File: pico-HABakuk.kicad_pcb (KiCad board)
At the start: 2 copper layers, 52 x 51.2 mm, 90 parts, among them J1 USB_B_Micro, J2 Ant+, J3 GPS Ant, J4 Ant-, J5 Solar, J6 Debug, J7 Super_Cap, Q1 BSS84, SW1 USB BOOT, SW2 RESET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

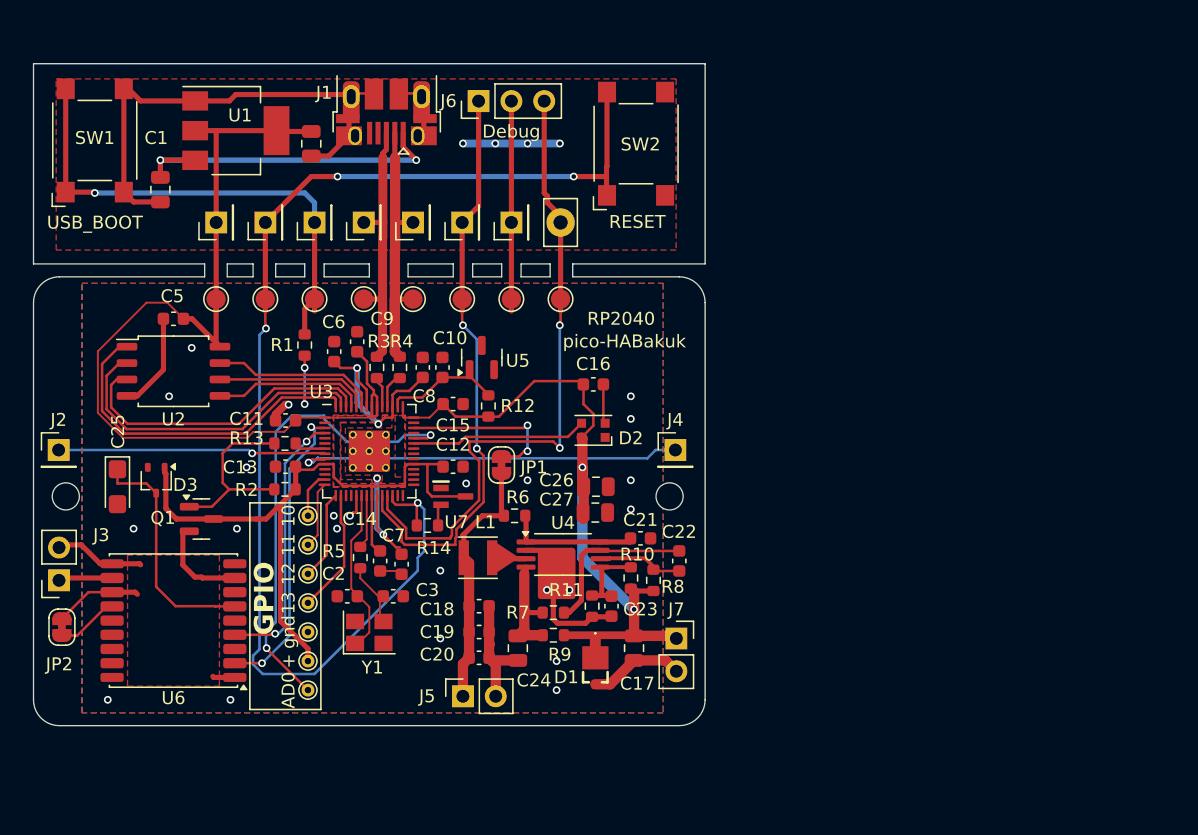
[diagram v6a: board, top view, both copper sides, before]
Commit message: Minor silkscreen edits
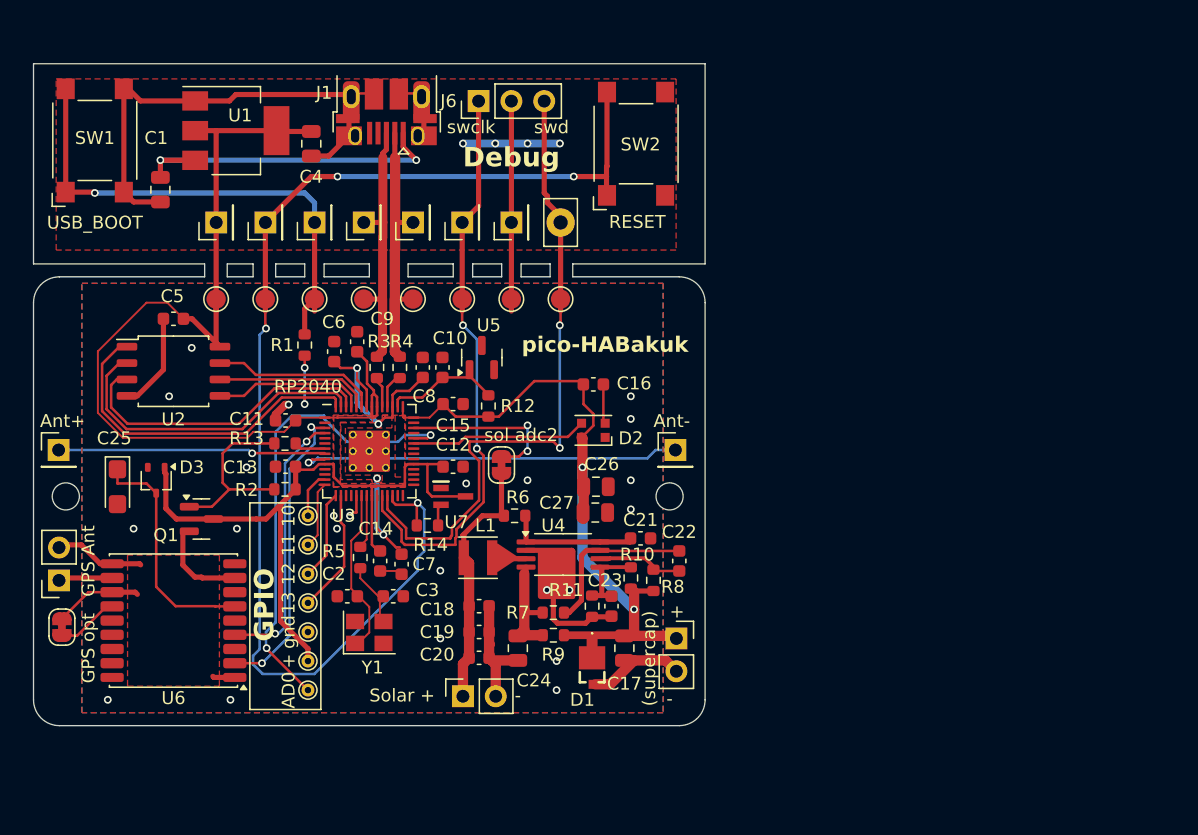
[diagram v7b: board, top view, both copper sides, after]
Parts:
- JP1: value Solar_voltage -> sol adc2
- JP2: value GPS+Glonass -> GPS opt
- moved C17 0.75 mm to (119.8, 115.2)
- moved D1 0.25 mm to (117.2, 116.0)
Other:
- rule pad_to_mask_clearance: 0.051 -> 0
- board text added: "(supercap)"
- board text added: "Solar +"
- board text added: "swclk"
- board text added: "swd"
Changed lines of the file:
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@@
 	)
 	(setup
-		(pad_to_mask_clearance 0.051)
-		(solder_mask_min_width 0.09)
+		(pad_to_mask_clearance 0)
 		(allow_soldermask_bridges_in_footprints no)
 		(aux_axis_origin 100 100)
@@
 			(disableapertmacros no)
 			(usegerberextensions no)
-			(usegerberattributes no)
+			(usegerberattributes yes)
 			(usegerberadvancedattributes no)
 			(creategerberjobfile no)
@@
 		(tags "capacitor")
 		(property "Reference" "C4"
-			(at 0 1.7 90)
+			(at 2.555 0.008 180)
 			(layer "F.SilkS")
-			(hide yes)
 			(effects
 				(font
@@
 		(tags "capacitor")
 		(property "Reference" "C14"
-			(at -3.25 1.588 0)
+			(at -2.5 0.338 0)
 			(layer "F.SilkS")
 			(effects
@@
 		(tags "capacitor")
 		(property "Reference" "C7"
-			(at -2.219 0.62 0)
+			(at 0 -1.75 0)
 			(layer "F.SilkS")
 			(effects
@@
 		(tags "capacitor")
 		(property "Reference" "C16"
-			(at 0 -1.578 0)
+			(at 3.152 -0.078 0)
 			(layer "F.SilkS")
 			(effects
@@
 		(tags "QFN DFN_QFN")
 		(property "Reference" "U3"
-			(at -3.71 -4.6 0)
+			(at -2 5 0)
 			(layer "F.SilkS")
 			(effects
@@
 	(footprint "Capacitor_SMD:C_0805_2012Metric"
 		(layer "F.Cu")
-		(at 120.5 115.25 -90)
+		(at 119.75 115.25 -90)
 		(descr "Capacitor SMD 0805 (2012 Metric), square (rectangular) end terminal, IPC_7351 nominal, (Body size source: IPC-SM-782 page 76, https://www.pcb-3d.com/wordpress/wp-content/uploads/ipc-sm-782a_amendment_1_and_2.pdf, https://docs.google.com/spreadsheets/d/1BsfQQcO9C6DZCsRaXUlFlo91Tg2WpOkGARC1WS5S8t0/edit?usp=sharing), generated with kicad-footprint-generator")
 		(tags "capacitor")
 		(property "Reference" "C17"
-			(at 2.75 -0.25 180)
+			(at 2.75 0 180)
 			(layer "F.SilkS")
 			(effects
@@
 		(tags "inductor taiyo-yuden md smd")
 		(property "Reference" "L1"
-			(at 0.586 -2.75 0)
+			(at 0.586 -2.5 0)
 			(layer "F.SilkS")
 			(effects
@@
 		(tags "resistor")
 		(property "Reference" "R9"
-			(at -0.5 -1.5 0)
+			(at 0 -1.5 0)
 			(layer "F.SilkS")
 			(effects
@@
 		(tags "net tie solder jumper bridged")
 		(property "Reference" "JP1"
-			(at -0.184 2.514 180)
+			(at 0.566 2.764 360)
 			(layer "F.SilkS")
+			(hide yes)
 			(effects
 				(font
@@
 			)
 		)
-		(property "Value" "Solar_voltage"
-			(at 0 1.9 90)
-			(layer "F.Fab")
+		(property "Value" "sol adc2"
+			(at 2.316 1.514 360)
+			(layer "F.SilkS")
 			(effects
 				(font
@@
 		(tags "SOT TO_SOT_SMD")
 		(property "Reference" "Q1"
-			(at -2.976 -0.086 0)
+			(at -2.75 1.25 0)
 			(layer "F.SilkS")
 			(effects
@@
 		(tags "capacitor tantalum")
 		(property "Reference" "C25"
-			(at -4.274 -0.05 90)
+			(at -3.75 0.25 180)
 			(layer "F.SilkS")
 			(effects
@@
 			(at 0 -2.33 0)
 			(layer "F.SilkS")
+			(hide yes)
 			(effects
 				(font
@@
 		(tags "capacitor")
 		(property "Reference" "C26"
-			(at -3.05 -0.5 0)
+			(at 0.45 -1.75 0)
 			(layer "F.SilkS")
 			(effects
@@
 			(at 0 -2.33 0)
 			(layer "F.SilkS")
+			(hide yes)
 			(effects
 				(font
@@
 			(at 0 -2.25 0)
 			(layer "F.SilkS")
+			(hide yes)
 			(effects
 				(font
@@
 		(tags "capacitor")
 		(property "Reference" "C23"
-			(at 0.25 -2.25 180)
+			(at -2 0.5 180)
 			(layer "F.SilkS")
 			(effects
@@
 		(tags "net tie solder jumper bridged")
 		(property "Reference" "JP2"
-			(at 2.876 0.2 180)
+			(at 2.876 0.2 360)
 			(layer "F.SilkS")
+			(hide yes)
 			(effects
 				(font
@@
 			)
 		)
-		(property "Value" "GPS+Glonass"
-			(at 0 1.9 90)
-			(layer "F.Fab")
+		(property "Value" "GPS opt"
+			(at 1.626 -2.05 90)
+			(layer "F.SilkS")
 			(effects
 				(font
@@
 		(tags "TSSOP SO")
 		(property "Reference" "U4"
-			(at 0 -2.45 0)
+			(at -0.75 -2.25 0)
 			(layer "F.SilkS")
 			(effects
@@
 		(tags "resistor")
 		(property "Reference" "R14"
-			(at 0.5 1.75 0)
+			(at 0.25 1.5 0)
 			(layer "F.SilkS")
 			(effects
@@
 			(at -3.275 3.5 0)
 			(layer "F.SilkS")
+			(hide yes)
 			(effects
 				(font
@@
 		)
 		(property "Value" "GPS Ant"
-			(at 0 5.31 0)
-			(layer "F.Fab")
+			(at -2.275 1.5 90)
+			(layer "F.SilkS")
 			(effects
 				(font
@@
 		(tags "SOT TO_SOT_SMD")
 		(property "Reference" "U5"
-			(at -0.25 2.788 180)
+			(at 2.5 0.538 180)
 			(layer "F.SilkS")
 			(effects
@@
 		)
 		(property "Value" "Debug"
-			(at -2.357 2.538 180)
+			(at -4.357 2.538 180)
 			(layer "F.SilkS")
 			(effects
 				(font
-					(size 1 1)
-					(thickness 0.15)
+					(size 1.5 1.5)
+					(thickness 0.3)
+					(bold yes)
 				)
 			)
@@
 		(tags "SOT-323 SC-70")
 		(property "Reference" "D3"
-			(at 0.364 -2.258 0)
+			(at -1 -2.75 0)
 			(layer "F.SilkS")
 			(effects
@@
 			(at 0 -2.77 180)
 			(layer "F.SilkS")
+			(hide yes)
 			(effects
 				(font
@@
 		(tags "capacitor")
 		(property "Reference" "C27"
-			(at -3 -1 0)
+			(at -3 -0.75 0)
 			(layer "F.SilkS")
 			(effects
@@
 	(footprint "SamacSys_Parts:SMM4F15ATR"
 		(layer "F.Cu")
-		(at 117.5 116 90)
+		(at 117.25 116 90)
 		(descr "STmite_2022")
 		(tags "Zener Diode")
 		(property "Reference" "D1"
-			(at -1.5 -2.25 180)
+			(at -3.25 -0.75 180)
 			(layer "F.SilkS")
 			(effects
@@
 	)
 	(gr_text "RP2040"
-		(at 119.5 89.75 0)
+		(at 95.25 95 0)
 		(layer "F.SilkS")
 		(effects
@@
 	)
 	(gr_text "pico-HABakuk"
-		(at 119.75 91.5 0)
+		(at 118.25 91.75 0)
+		(layer "F.SilkS")
+		(effects
+			(font
+				(size 1.2 1.2)
+				(thickness 0.25)
+				(bold yes)
+			)
+		)
+	)
+	(gr_text "swclk"
+		(at 106 75.5 0)
+		(layer "F.SilkS")
+		(effects
+			(font
+				(size 1 1)
+				(thickness 0.15)
+			)
+			(justify left bottom)
+		)
+	)
+	(gr_text "(supercap)"
+		(at 122.25 119.75 90)
 		(layer "F.SilkS")
 		(effects
@@
 				(thickness 0.15)
 			)
+			(justify left bottom)
 		)
 	)
 	(gr_text "GPIO"
-		(at 92.75 114.25 90)
+		(at 92.75 114.75 90)
 		(layer "F.SilkS")
 		(effects
@@
 		)
 	)
+	(gr_text "Ant+"
+		(at 74.5 98.25 0)
+		(layer "F.SilkS")
+		(effects
+			(font
+				(size 1 1)
+				(thickness 0.15)
+			)
+			(justify left bottom)
+		)
+	)
+	(gr_text "+"
+		(at 123.25 113 0)
+		(layer "F.SilkS")
+		(effects
+			(font
+				(size 1 1)
+				(thickness 0.15)
+			)
+			(justify left bottom)
+		)
+	)
 	(gr_text "\nUSB_BOOT"
 		(at 78.75 81.5 0)
@@
 		)
 	)
+	(gr_text "swd"
+		(at 112.75 75.5 0)
+		(layer "F.SilkS")
+		(effects
+			(font
+				(size 1 1)
+				(thickness 0.15)
+			)
+			(justify left bottom)
+		)
+	)
+	(gr_text "-"
+		(at 111.25 119.5 0)
+		(layer "F.SilkS")
+		(effects
+			(font
+				(size 1 1)
+				(thickness 0.15)
+			)
+			(justify left bottom)
+		)
+	)
+	(gr_text "Solar +"
+		(at 100 119.5 0)
+		(layer "F.SilkS")
+		(effects
+			(font
+				(size 1 1)
+				(thickness 0.15)
+			)
+			(justify left bottom)
+		)
+	)
+	(gr_text "-"
+		(at 123 119.75 0)
+		(layer "F.SilkS")
+		(effects
+			(font
+				(size 1 1)
+				(thickness 0.15)
+			)
+			(justify left bottom)
+		)
+	)
+	(gr_text "Ant-"
+		(at 122 98.25 0)
+		(layer "F.SilkS")
+		(effects
+			(font
+				(size 1 1)
+				(thickness 0.15)
+			)
+			(justify left bottom)
+		)
+	)
